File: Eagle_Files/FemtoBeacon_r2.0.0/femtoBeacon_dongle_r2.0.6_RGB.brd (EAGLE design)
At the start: 39.4 x 27.9 mm, 44 parts

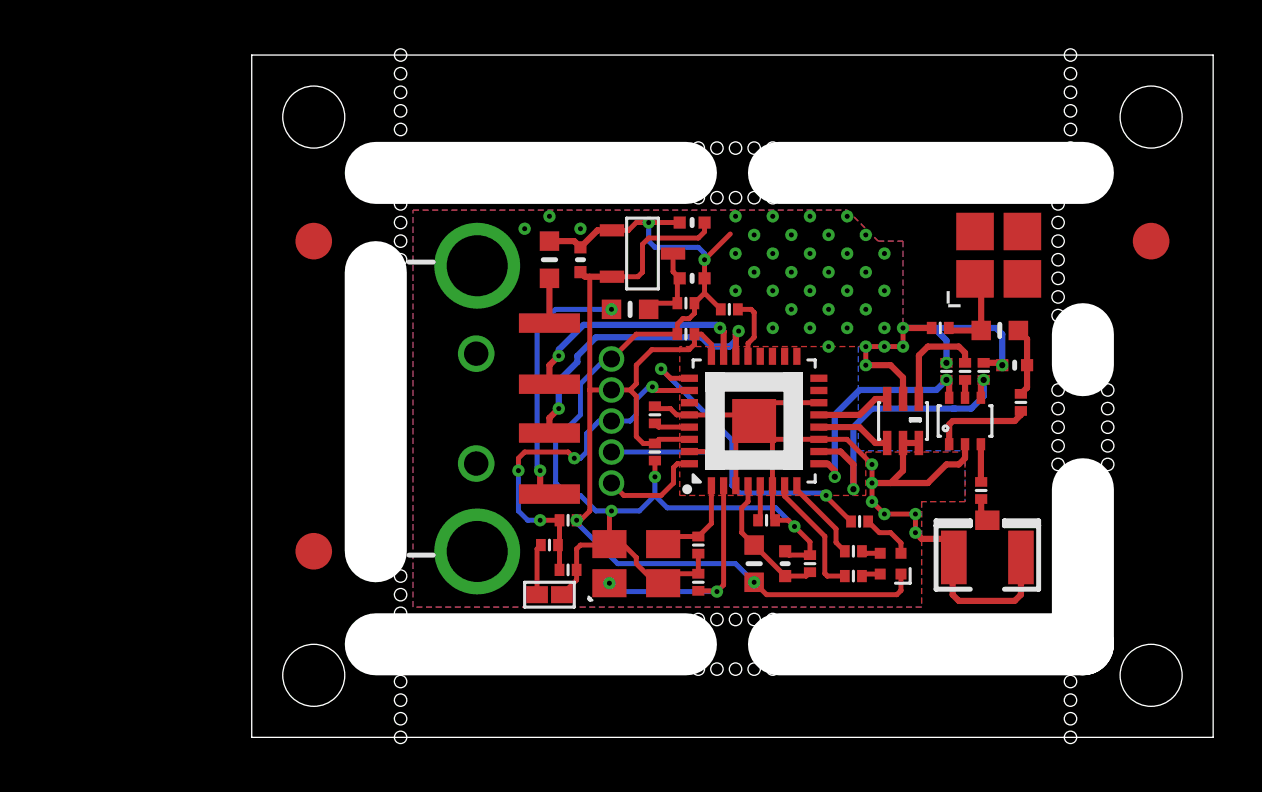
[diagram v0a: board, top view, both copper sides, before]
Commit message: Adding initial Taiyo Yuden BT5 module based FemtoBeacon revision 2.0.0 design, adding FemtoBeacon Dongle r2.0.6 solder paste/stencil jig (Blender 3D, Cura slice) and FemtoBeacon coin r2.0.7 solder paste/stencil jig (Cura slice, the Blender 3D model was added in an earlier commit). Adding panelized femtoBeacon r2.0.7 coins, and panelized femtoBeacon dongles r2.0.6
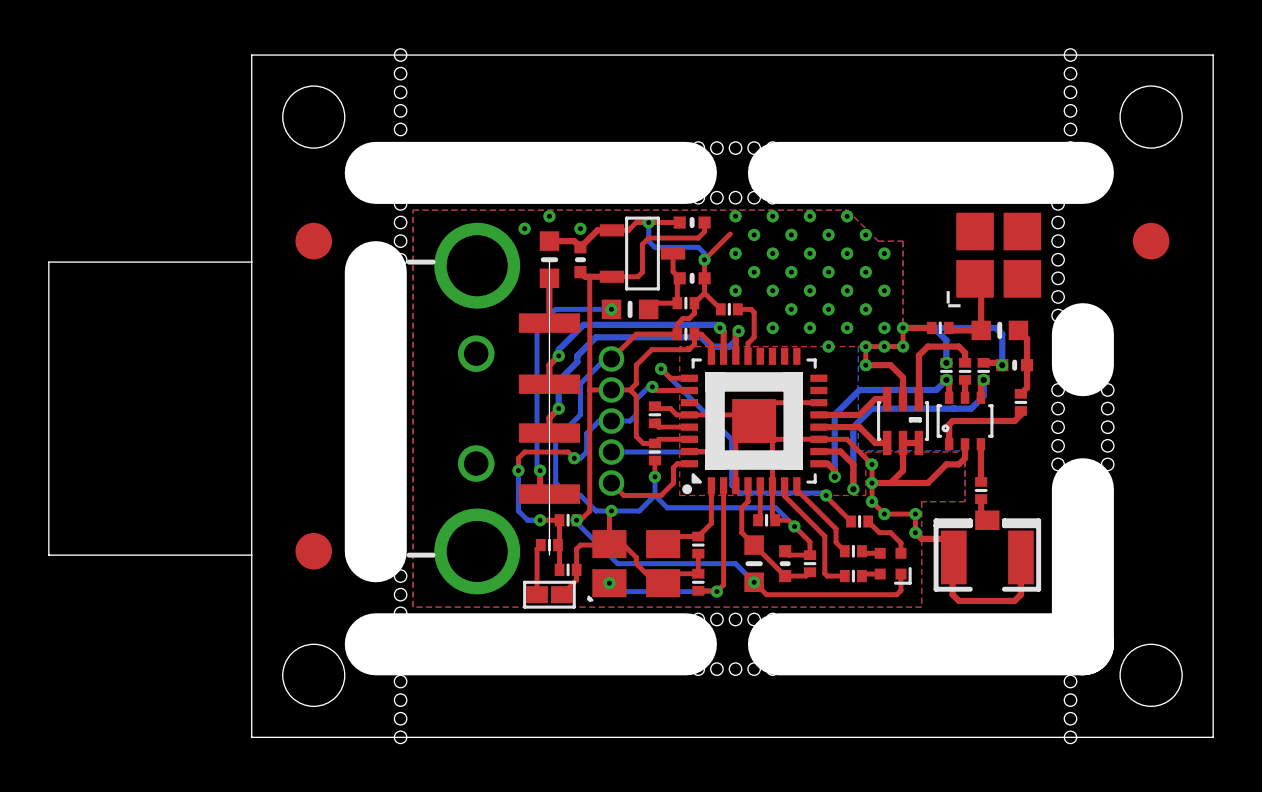
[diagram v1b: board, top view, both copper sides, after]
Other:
- board size 39.4 x 27.9 mm -> 47.7 x 27.9 mm
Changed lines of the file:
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@@
 <setting verticaltext="up"/>
 </settings>
-<grid distance="50" unitdist="mil" unit="mil" style="lines" multiple="1" display="yes" altdistance="0.025" altunitdist="inch" altunit="inch"/>
+<grid distance="1" unitdist="mm" unit="mm" style="lines" multiple="1" display="yes" altdistance="0.025" altunitdist="inch" altunit="inch"/>
 <layers>
 <layer number="1" name="Top" color="4" fill="1" visible="yes" active="yes"/>
@@
 <wire x1="39.37" y1="0" x2="39.37" y2="27.94" width="0" layer="20"/>
 <wire x1="39.37" y1="27.94" x2="0" y2="27.94" width="0" layer="20"/>
-<wire x1="0" y1="27.94" x2="0" y2="0" width="0" layer="20"/>
+<wire x1="0" y1="27.94" x2="0" y2="19.462" width="0" layer="20"/>
 <hole x="2.54" y="2.54" drill="2.54"/>
 <hole x="2.54" y="25.4" drill="2.54"/>
@@
 <hole x="33.02" y="18.796" drill="0.508"/>
 <hole x="33.02" y="18.034" drill="0.508"/>
+<wire x1="0" y1="19.462" x2="0" y2="7.462" width="0" layer="20"/>
+<wire x1="0" y1="7.462" x2="0" y2="0" width="0" layer="20"/>
 <wire x1="34.036" y1="15.24" x2="34.036" y2="16.51" width="2.54" layer="46"/>
 <hole x="33.02" y="17.272" drill="0.508"/>
+<dimension x1="0" y1="27.94" x2="39.37" y2="27.94" x3="19.685" y3="31.75" textsize="1.778" layer="51" visible="yes"/>
+<dimension x1="39.37" y1="27.94" x2="39.37" y2="0" x3="44.45" y3="13.97" textsize="1.778" layer="51" visible="yes"/>
+<dimension x1="2.54" y1="1.27" x2="2.54" y2="3.81" x3="-15.24" y3="2.54" textsize="1.778" layer="51" dtype="diameter" visible="yes"/>
+<dimension x1="2.54" y1="2.54" x2="0" y2="2.54" x3="1.27" y3="-5.08" textsize="1.778" layer="51" visible="yes"/>
+<dimension x1="36.83" y1="2.54" x2="0" y2="2.54" x3="18.415" y3="-8.89" textsize="1.778" layer="51" visible="yes"/>
+<dimension x1="2.54" y1="25.4" x2="2.54" y2="0" x3="-20.32" y3="12.7" textsize="1.778" layer="51" visible="yes"/>
+<wire x1="36.83" y1="2.54" x2="36.83" y2="25.4" width="0.254" layer="51" style="shortdash"/>
+<wire x1="2.54" y1="25.4" x2="36.83" y2="25.4" width="0.254" layer="51" style="shortdash"/>
+<wire x1="12.192" y1="7.462" x2="12.192" y2="19.462" width="0" layer="20"/>
+<wire x1="-8.308" y1="7.462" x2="-8.308" y2="19.462" width="0" layer="20"/>
+<wire x1="-8.308" y1="19.462" x2="0" y2="19.462" width="0" layer="20"/>
+<dimension x1="0" y1="19.462" x2="-8.308" y2="19.462" x3="-4.154" y3="39.751" textsize="1.778" layer="51" visible="yes"/>
+<wire x1="-8.308" y1="7.462" x2="0" y2="7.462" width="0" layer="20"/>
+<dimension x1="0" y1="7.462" x2="-8.308" y2="7.462" x3="-4.154" y3="-13" textsize="1.778" layer="51" visible="yes"/>
 </plain>
 <attributes>
